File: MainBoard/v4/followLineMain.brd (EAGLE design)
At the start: 95 x 53.1 mm, 32 parts, among them IC1 L298, J1 DCJ0202, X1 332-02, X2 332-02

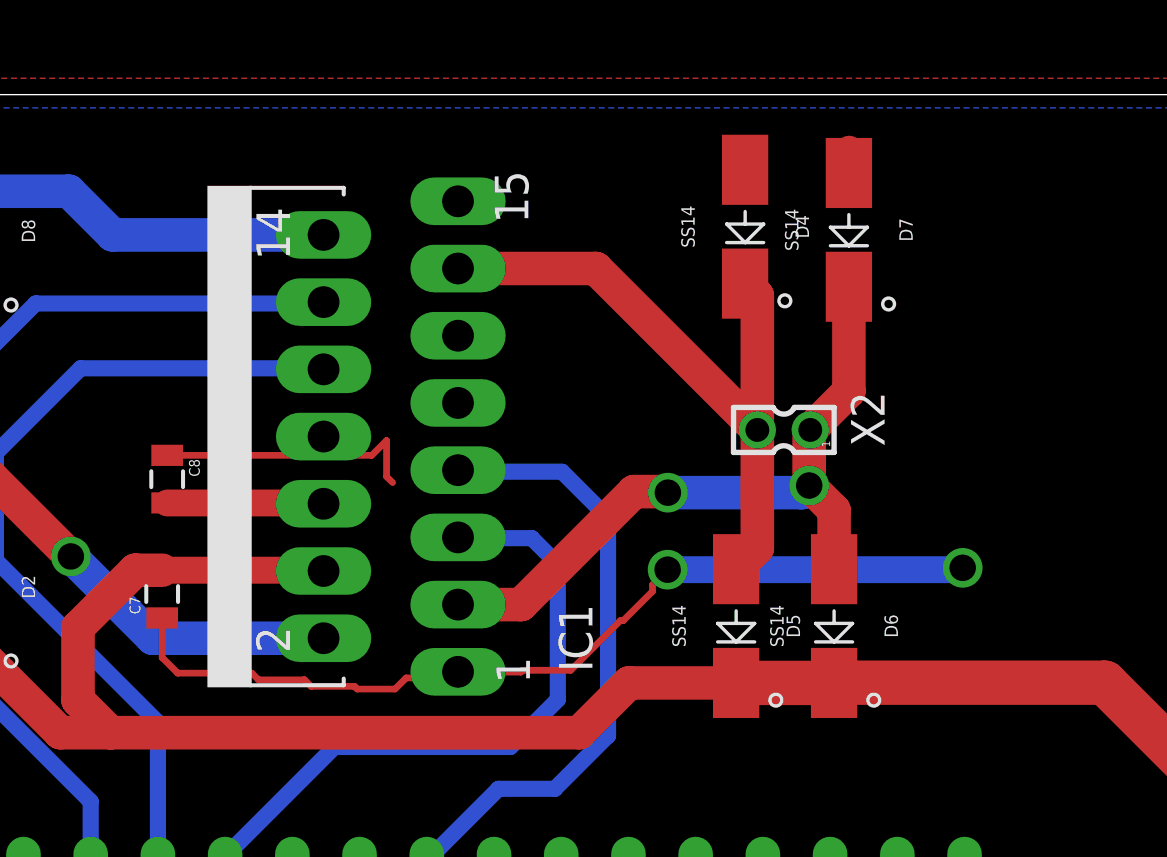
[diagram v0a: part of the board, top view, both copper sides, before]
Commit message: Improved the ground trace to the H-bridge
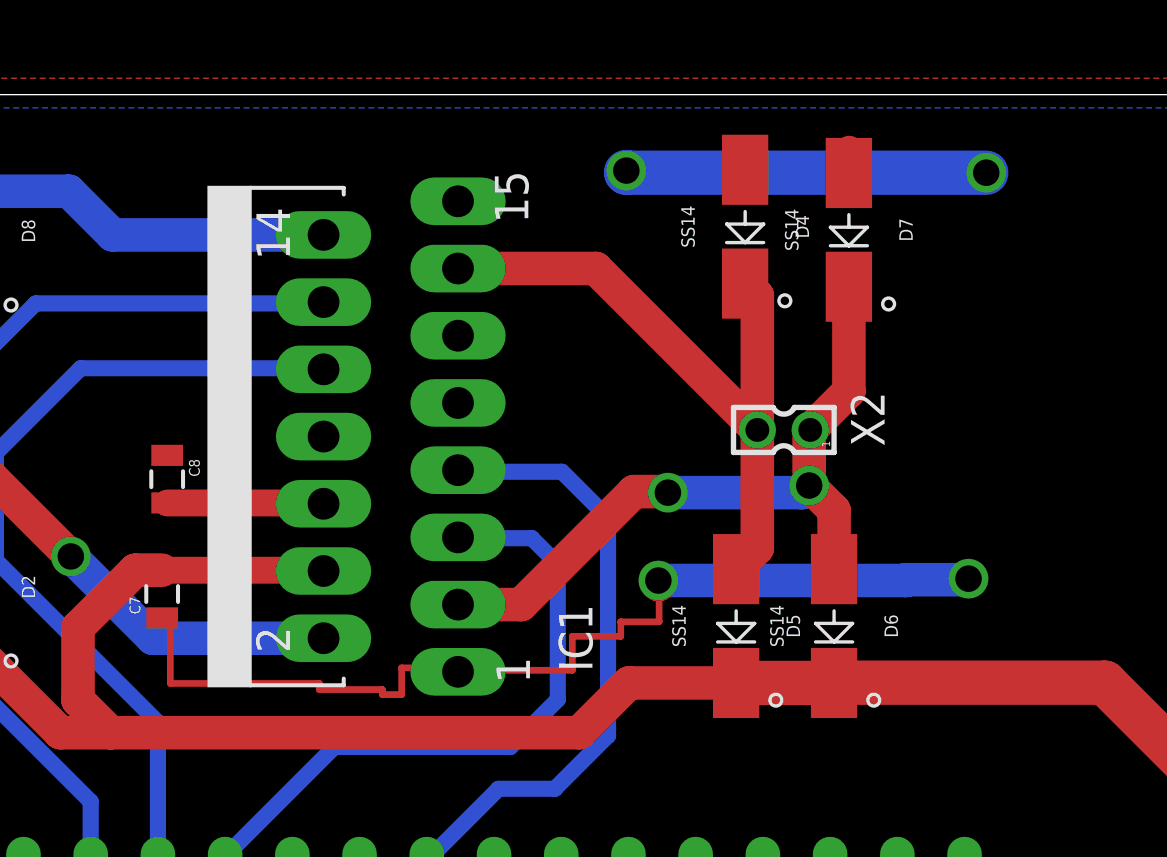
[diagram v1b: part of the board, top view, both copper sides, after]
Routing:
- net GND: track 71.0 -> 78.1 mm, vias 5 -> 7
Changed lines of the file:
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@@
 <wire x1="69.19" y1="2.51" x2="69.26" y2="2.58" width="0.6096" layer="16"/>
 <via x="69.26" y="2.58" extent="1-16" drill="1" shape="square"/>
-<via x="55.91" y="35.26" extent="1-16" drill="1" shape="square"/>
-<wire x1="25.85" y1="39.51" x2="33.58" y2="39.51" width="0.254" layer="1"/>
-<wire x1="33.58" y1="39.51" x2="34.14" y2="40.07" width="0.254" layer="1"/>
-<wire x1="34.14" y1="40.07" x2="34.14" y2="38.71" width="0.254" layer="1"/>
-<wire x1="34.14" y1="38.71" x2="34.37" y2="38.48" width="0.254" layer="1"/>
-<wire x1="25.66" y1="33.37" x2="25.66" y2="31.87" width="0.254" layer="1"/>
-<wire x1="25.66" y1="31.87" x2="26.25" y2="31.28" width="0.254" layer="1"/>
-<wire x1="26.25" y1="31.28" x2="29.05" y2="31.28" width="0.254" layer="1"/>
-<wire x1="29.05" y1="31.28" x2="29.3" y2="31.03" width="0.254" layer="1"/>
-<wire x1="29.3" y1="31.03" x2="31.04" y2="31.03" width="0.254" layer="1"/>
-<wire x1="31.04" y1="31.03" x2="31.29" y2="30.78" width="0.254" layer="1"/>
-<wire x1="31.29" y1="30.78" x2="32.93" y2="30.78" width="0.254" layer="1"/>
-<wire x1="32.93" y1="30.78" x2="33.03" y2="30.68" width="0.254" layer="1"/>
-<wire x1="33.03" y1="30.68" x2="34.46" y2="30.68" width="0.254" layer="1"/>
-<wire x1="34.46" y1="30.68" x2="34.88" y2="31.1" width="0.254" layer="1"/>
-<wire x1="34.88" y1="31.1" x2="35.2" y2="31.1" width="0.254" layer="1"/>
-<wire x1="35.2" y1="31.1" x2="35.45" y2="31.35" width="0.254" layer="1"/>
-<wire x1="35.45" y1="31.35" x2="37.09" y2="31.35" width="0.254" layer="1"/>
-<wire x1="37.09" y1="31.35" x2="37.12" y2="31.32" width="0.254" layer="1"/>
-<wire x1="37.12" y1="31.32" x2="39.22" y2="31.32" width="0.254" layer="1"/>
-<wire x1="39.22" y1="31.32" x2="39.29" y2="31.39" width="0.254" layer="1"/>
-<wire x1="39.29" y1="31.39" x2="41.1" y2="31.39" width="0.254" layer="1"/>
-<wire x1="41.1" y1="31.39" x2="42.98" y2="33.27" width="0.254" layer="1"/>
-<wire x1="42.98" y1="33.27" x2="43.09" y2="33.27" width="0.254" layer="1"/>
-<wire x1="43.09" y1="33.27" x2="44.19" y2="34.37" width="0.254" layer="1"/>
-<wire x1="44.19" y1="34.37" x2="44.19" y2="34.62" width="0.254" layer="1"/>
-<wire x1="44.19" y1="34.62" x2="44.76" y2="35.19" width="0.254" layer="1"/>
-<via x="44.76" y="35.19" extent="1-16" drill="1" shape="square"/>
-<wire x1="44.76" y1="35.19" x2="55.84" y2="35.19" width="1.016" layer="16"/>
-<wire x1="55.84" y1="35.19" x2="55.91" y2="35.26" width="0.254" layer="16"/>
 <wire x1="88.72" y1="14.59" x2="88.7" y2="14.59" width="0.6096" layer="16"/>
 <wire x1="88.7" y1="14.59" x2="87.27" y2="16.02" width="0.6096" layer="16"/>
@@
 <wire x1="85.88" y1="17.43" x2="85.41" y2="17.43" width="0.6096" layer="16"/>
 <wire x1="85.41" y1="17.43" x2="85.31" y2="17.53" width="0.6096" layer="16"/>
+<via x="43.2" y="50.27" extent="1-16" drill="1" shape="square"/>
+<via x="56.8" y="50.19" extent="1-16" drill="1" shape="square"/>
+<wire x1="56.8" y1="50.19" x2="43.2" y2="50.19" width="1.6764" layer="16"/>
+<wire x1="43.2" y1="50.19" x2="43.2" y2="50.22" width="1.6764" layer="16"/>
+<wire x1="25.66" y1="33.37" x2="25.97" y2="33.37" width="0.254" layer="1"/>
+<wire x1="25.97" y1="33.37" x2="25.97" y2="30.89" width="0.254" layer="1"/>
+<wire x1="25.97" y1="30.89" x2="31.6" y2="30.89" width="0.254" layer="1"/>
+<wire x1="31.6" y1="30.89" x2="31.6" y2="30.66" width="0.254" layer="1"/>
+<wire x1="31.6" y1="30.66" x2="33.98" y2="30.66" width="0.254" layer="1"/>
+<wire x1="33.98" y1="30.66" x2="33.98" y2="30.47" width="0.254" layer="1"/>
+<wire x1="33.98" y1="30.47" x2="34.71" y2="30.47" width="0.254" layer="1"/>
+<wire x1="34.71" y1="30.47" x2="34.71" y2="31.48" width="0.254" layer="1"/>
+<wire x1="34.71" y1="31.48" x2="36.08" y2="31.48" width="0.254" layer="1"/>
+<wire x1="36.08" y1="31.48" x2="36.08" y2="31.44" width="0.254" layer="1"/>
+<wire x1="36.08" y1="31.44" x2="37.45" y2="31.44" width="0.254" layer="1"/>
+<wire x1="37.45" y1="31.44" x2="37.45" y2="31.39" width="0.254" layer="1"/>
+<wire x1="37.45" y1="31.39" x2="41.16" y2="31.39" width="0.254" layer="1"/>
+<wire x1="41.16" y1="31.39" x2="41.16" y2="32.67" width="0.254" layer="1"/>
+<wire x1="41.16" y1="32.67" x2="42.99" y2="32.67" width="0.254" layer="1"/>
+<wire x1="42.99" y1="32.67" x2="42.99" y2="33.22" width="0.254" layer="1"/>
+<wire x1="42.99" y1="33.22" x2="44.44" y2="33.22" width="0.254" layer="1"/>
+<wire x1="44.44" y1="33.22" x2="44.44" y2="34.63" width="0.254" layer="1"/>
+<wire x1="44.44" y1="34.63" x2="44.41" y2="34.63" width="1.27" layer="1"/>
+<wire x1="44.41" y1="34.63" x2="44.41" y2="34.78" width="1.27" layer="1"/>
+<via x="44.41" y="34.78" extent="1-16" drill="1" shape="square"/>
+<wire x1="44.41" y1="34.78" x2="53.76" y2="34.78" width="1.27" layer="16"/>
+<wire x1="53.76" y1="34.78" x2="53.76" y2="34.81" width="1.27" layer="16"/>
+<wire x1="53.76" y1="34.81" x2="56.13" y2="34.81" width="1.27" layer="16"/>
+<wire x1="56.13" y1="34.81" x2="56.13" y2="34.85" width="1.27" layer="16"/>
+<via x="56.13" y="34.85" extent="1-16" drill="1" shape="square"/>
 </signal>
 <signal name="OUT4">

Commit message: Minor changes on brd main file
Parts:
- moved LED16 5.08 mm to (66.8, 15.9)
- moved R19 5.08 mm to (83.2, 9.04)
- moved R25 5.08 mm to (48.1, 2.66)
- moved U$1 5.08 mm to (42.0, 18.7)
- moved C7 5.08 mm to (20.6, 34.2)
- moved C8 5.08 mm to (20.8, 38.6)
- moved SV1 5.08 mm to (28.0, 4.26)
- moved C1 5.08 mm to (2.29, 10.2)
- moved D1 5.08 mm to (9.56, 34.5)
- moved D2 5.08 mm to (13.4, 34.5)
- moved D3 5.08 mm to (9.56, 47.9)
- moved D8 5.08 mm to (13.4, 47.9)
- moved R1 5.08 mm to (10.7, 6.50)
- moved U$3 5.08 mm to (8.39, 12.3)
- moved X1 5.08 mm to (9.56, 41.4)
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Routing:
- net GND: track 78.1 -> 94.5 mm
- net 5V: track 7.83 -> 15.0 mm
- net VBAT: track 139.3 -> 137.6 mm

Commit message: Added another folder with our thoughts
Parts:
- moved C10 3.77 mm to (60.2, 7.51)
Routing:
- net 5V: track 15.0 -> 19.3 mm
- net VBAT: track 137.6 -> 133.9 mm
- net N$14: track 0.00 -> 1.83 mm
- net GND: track 94.5 -> 95.5 mm
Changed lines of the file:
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@@
 <attribute name="SPICEPREFIX" value="C" x="2.29" y="10.15" size="1.778" layer="28" rot="MR270" display="off"/>
 </element>
-<element name="C10" library="SparkFun-Capacitors" package="1206" value="1uF" x="61.14" y="3.86" rot="MR270"/>
+<element name="C10" library="SparkFun-Capacitors" package="1206" value="1uF" x="60.21" y="7.51" rot="MR270"/>
 <element name="C11" library="rcl" package="E5-13" value="330uF" x="73.13" y="42.69" rot="R90"/>
 <element name="C7" library="SparkFun-Capacitors" package="0805" value="100nF" x="20.58" y="34.22" rot="R90"/>
@@
 <wire x1="65.7" y1="9.08" x2="65.65" y2="9.03" width="1.27" layer="1"/>
 <via x="65.65" y="9.03" extent="1-16" drill="1" shape="square"/>
-<wire x1="65.65" y1="9.03" x2="65.65" y2="7.16" width="1.27" layer="16"/>
-<wire x1="65.65" y1="7.16" x2="64.79" y2="6.3" width="1.27" layer="16"/>
-<wire x1="64.79" y1="6.3" x2="64.79" y2="6.25" width="1.27" layer="16"/>
-<wire x1="64.79" y1="6.25" x2="63.75" y2="5.21" width="1.27" layer="16"/>
-<wire x1="63.75" y1="5.21" x2="61.19" y2="5.21" width="1.27" layer="16"/>
-<wire x1="61.19" y1="5.21" x2="61.14" y2="5.26" width="1.27" layer="16"/>
-<wire x1="61.14" y1="5.26" x2="58.49" y2="5.26" width="1.27" layer="16"/>
-<wire x1="58.49" y1="5.26" x2="55.31" y2="8.44" width="1.27" layer="16"/>
-<wire x1="55.31" y1="8.44" x2="50.96" y2="8.44" width="1.27" layer="16"/>
 <wire x1="50.96" y1="8.44" x2="50.9" y2="8.5" width="1.27" layer="16"/>
 <wire x1="69.66" y1="9.11" x2="65.73" y2="9.11" width="0.6096" layer="16"/>
@@
 <wire x1="13.37" y1="32.34" x2="15.27" y2="32.34" width="1.27" layer="1"/>
 <wire x1="15.27" y1="32.34" x2="17.4" y2="30.21" width="1.27" layer="1"/>
+<wire x1="60.21" y1="8.91" x2="65.65" y2="8.91" width="1.016" layer="16"/>
+<wire x1="65.65" y1="8.91" x2="65.65" y2="9.03" width="1.016" layer="16"/>
+<wire x1="60.21" y1="8.91" x2="51.31" y2="8.91" width="1.016" layer="16"/>
+<wire x1="51.31" y1="8.91" x2="50.9" y2="8.5" width="1.016" layer="16"/>
 </signal>
 <signal name="GND">
@@
 <wire x1="86.06" y1="12.12" x2="86.06" y2="10.99" width="0.6096" layer="16"/>
 <wire x1="86.06" y1="10.99" x2="84.11" y2="9.04" width="0.6096" layer="16"/>
-<wire x1="61.14" y1="2.46" x2="64.11" y2="2.46" width="0.6096" layer="16"/>
-<wire x1="64.11" y1="2.46" x2="64.18" y2="2.53" width="0.6096" layer="16"/>
-<via x="64.18" y="2.53" extent="1-16" drill="1" shape="square"/>
+<via x="64.1" y="5.97" extent="1-16" drill="1" shape="square"/>
 <wire x1="83.64" y1="14.54" x2="83.62" y2="14.54" width="0.6096" layer="16"/>
 <wire x1="83.62" y1="14.54" x2="82.19" y2="15.97" width="0.6096" layer="16"/>
@@
 <wire x1="21.74" y1="30.82" x2="31.3" y2="30.82" width="0.6096" layer="1"/>
 <wire x1="31.3" y1="30.82" x2="31.76" y2="31.28" width="0.6096" layer="1"/>
+<wire x1="64.1" y1="5.97" x2="60.21" y2="5.97" width="1.016" layer="16"/>
+<wire x1="60.21" y1="5.97" x2="60.21" y2="6.11" width="1.016" layer="16"/>
 </signal>
 <signal name="OUT4">
@@
 <wire x1="27.69" y1="37.6" x2="26.71" y2="37.6" width="0.8128" layer="16"/>
 <wire x1="26.71" y1="37.6" x2="26.68" y2="37.63" width="0.8128" layer="16"/>
-<wire x1="43.28" y1="8.5" x2="11.6412" y2="14.5606" width="0" layer="19" extent="1-1"/>
+<wire x1="43.28" y1="8.5" x2="43.25" y2="8.5" width="1.27" layer="16"/>
+<wire x1="43.25" y1="8.5" x2="43.25" y2="4.26" width="1.27" layer="16"/>
+<wire x1="43.25" y1="4.26" x2="45.32" y2="2.67" width="0" layer="19" extent="1-16"/>
 </signal>
 <signal name="VIN">
@@
 <signal name="N$13">
 </signal>
+<signal name="N$14">
+<wire x1="43.31" y1="8.45" x2="43.28" y2="8.45" width="1.27" layer="16"/>
+<wire x1="43.28" y1="8.45" x2="43.28" y2="6.65" width="1.27" layer="16"/>
+</signal>
 </signals>

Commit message: nothing changed...
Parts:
- moved X1 1.72 mm to (9.56, 39.7)
- moved C7 1.72 mm to (20.6, 32.5)
- moved C8 1.72 mm to (20.8, 36.8)
- moved D1 1.72 mm to (9.56, 32.8)
- moved D2 1.72 mm to (13.4, 32.8)
- moved D3 1.72 mm to (9.56, 46.2)
- moved D4 1.72 mm to (42.6, 46.4)
- moved D5 1.72 mm to (42.3, 31.3)
- moved D6 1.72 mm to (46.0, 31.3)
- moved D7 1.72 mm to (46.5, 46.3)
- moved D8 1.72 mm to (13.4, 46.2)
- moved IC1 1.72 mm to (24.1, 38.5)
- moved X2 1.72 mm to (44.1, 38.7)
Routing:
- net N$14: track 1.83 -> 0.00 mm
- net PWM3: track 32.1 -> 30.3 mm
- net PWM4: track 35.8 -> 34.7 mm
